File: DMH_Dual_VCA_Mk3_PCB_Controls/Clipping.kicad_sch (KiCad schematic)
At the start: 48 parts, among them Q10 BC548, Q11 BC548, Q12 BC548, Q9 BC548, SW2 SW_DPDT_OnOffOn_x2, U10 TL074

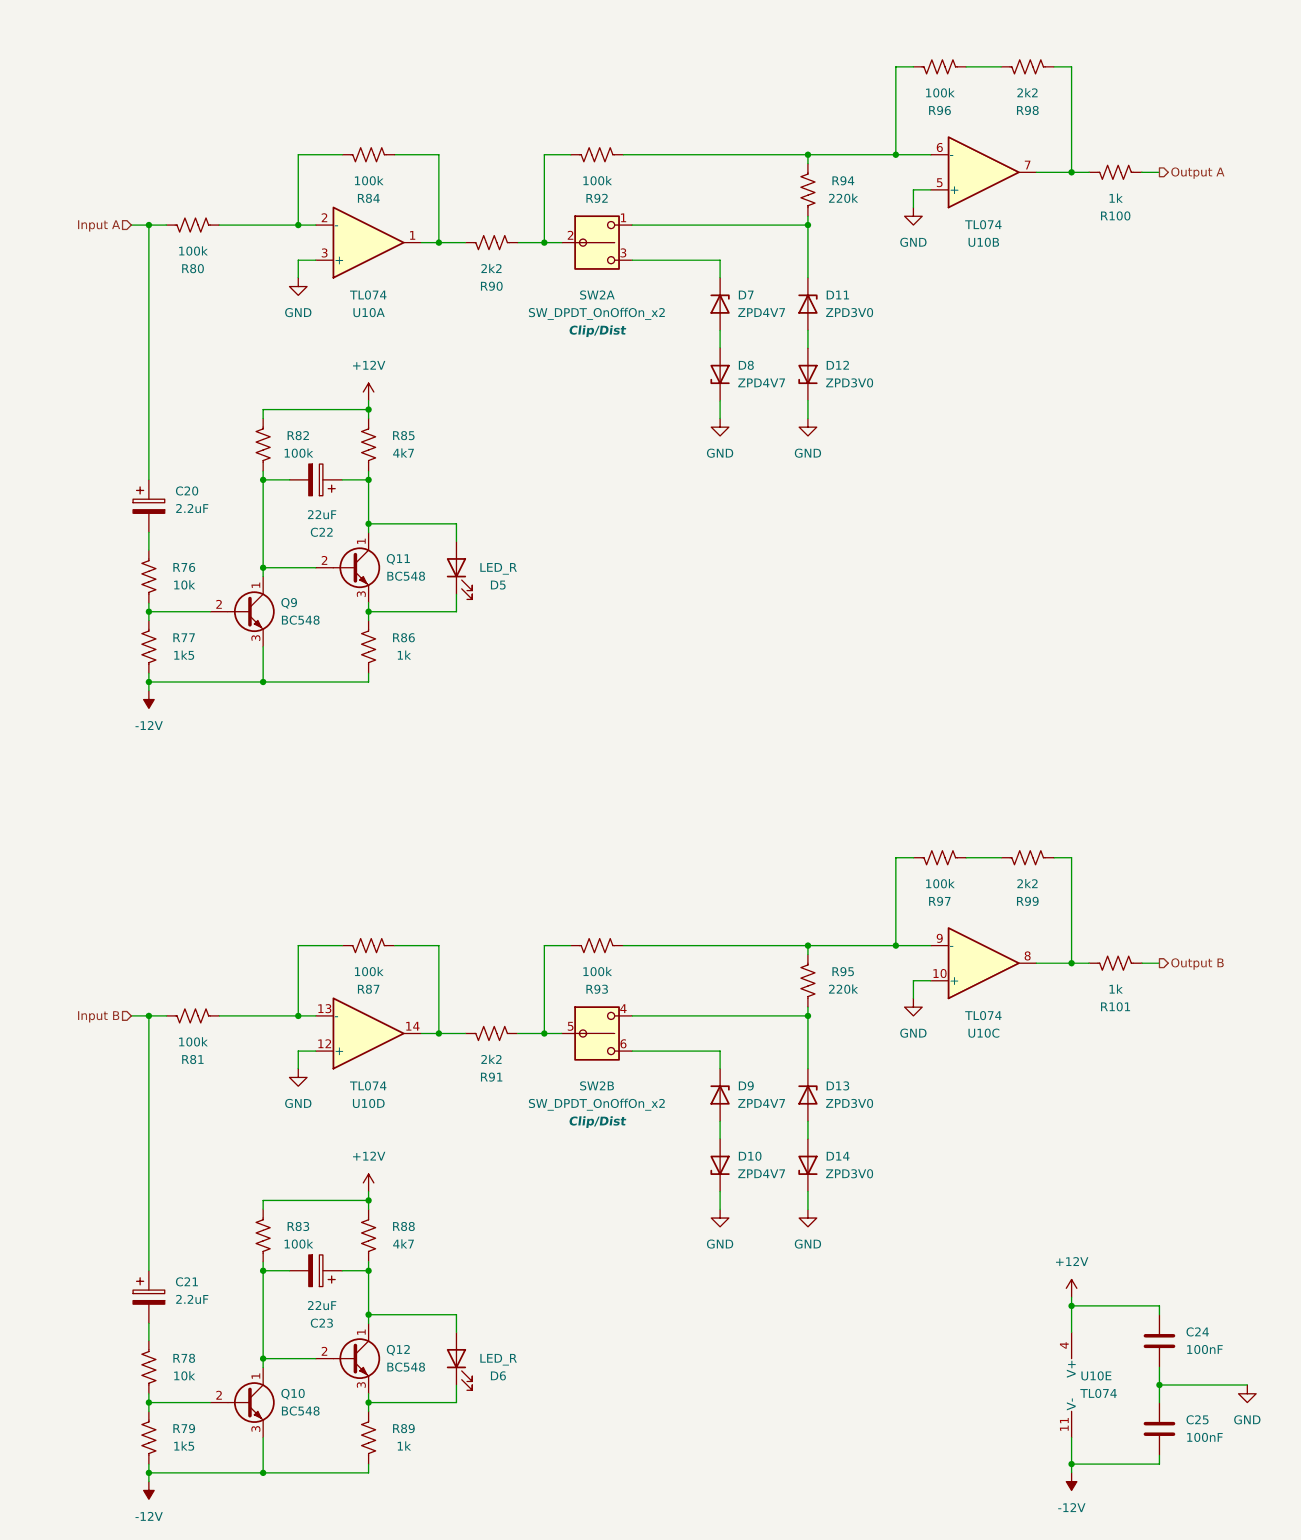
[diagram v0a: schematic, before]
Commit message: Moved clipping circuit back to main PCB
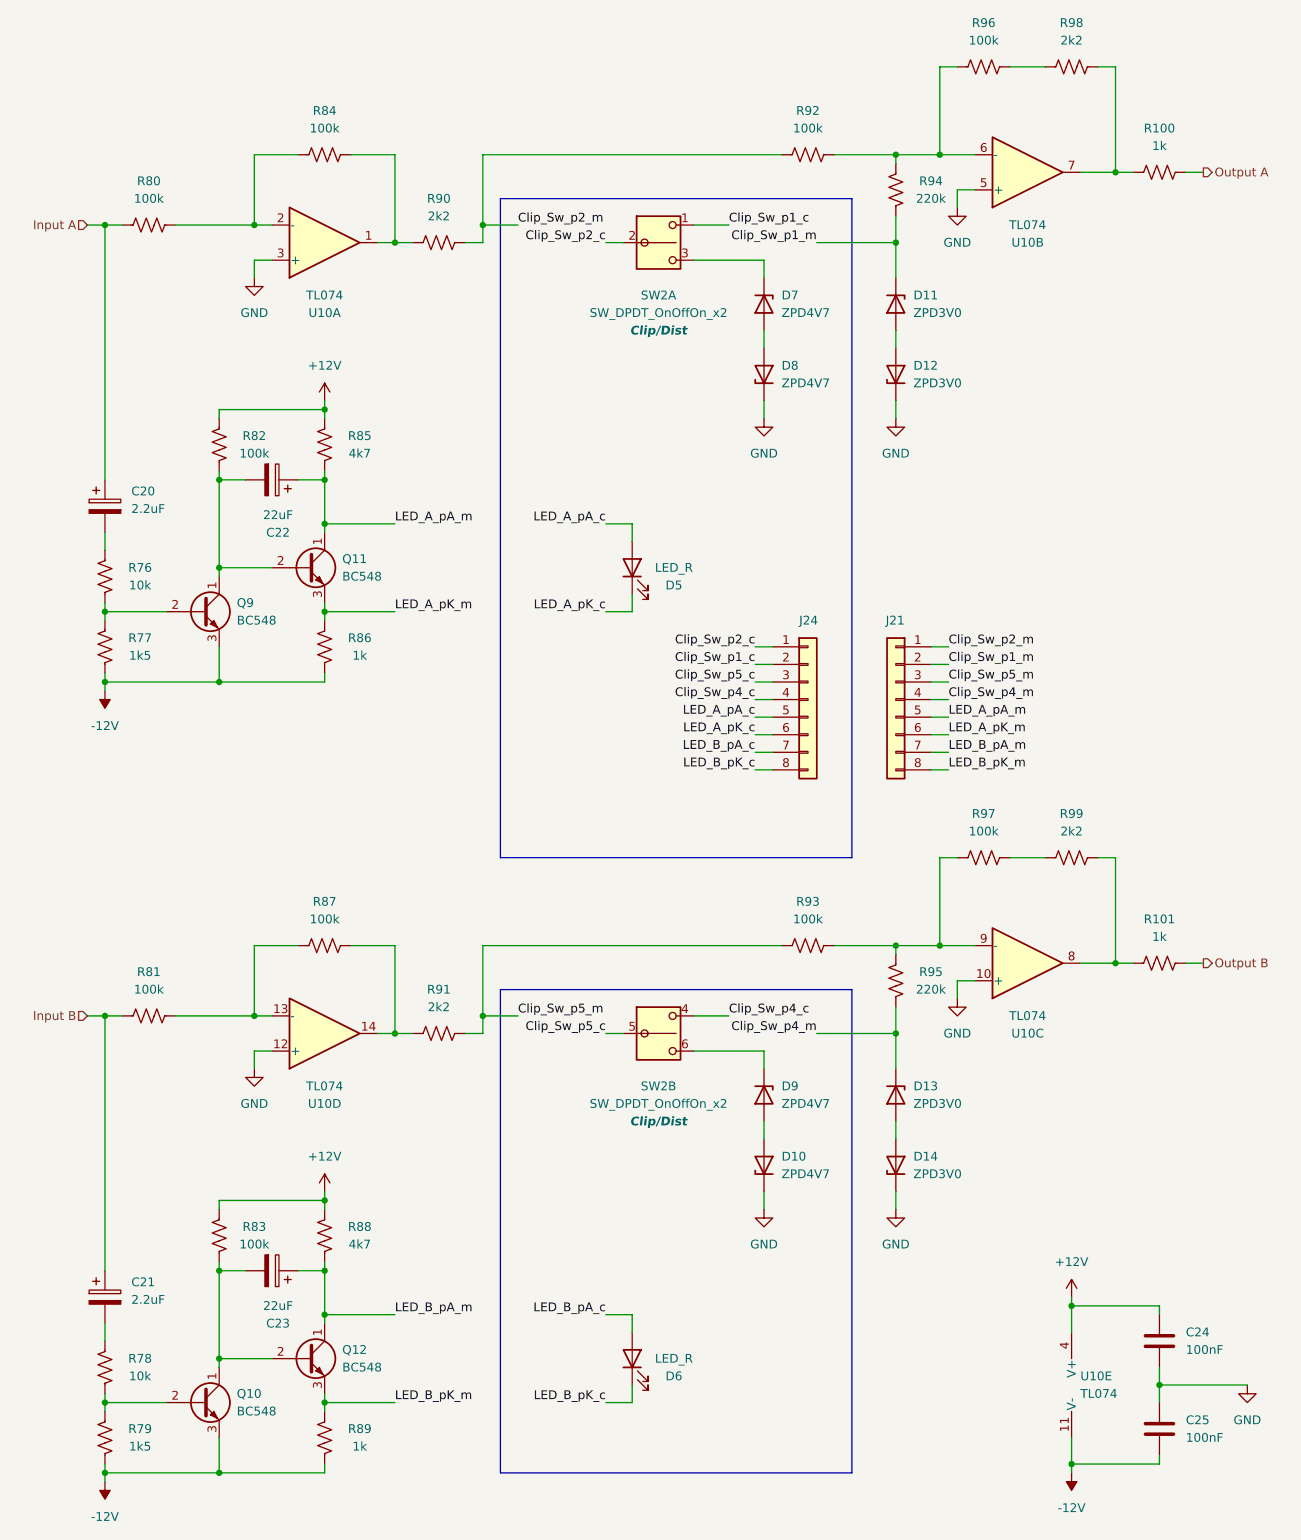
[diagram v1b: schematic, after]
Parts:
- added J21: Conn_01x08, Connector_PinHeader_2.54mm:PinHeader_1x08_P2.54mm_Vertical, symbol Connector_Generic:Conn_01x08
- added J24: Conn_01x08, Connector_PinSocket_2.54mm:PinSocket_1x08_P2.54mm_Vertical, symbol Connector_Generic:Conn_01x08
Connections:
- net Clip_Sw_p5_m: now reaches R91.2, R93.1
- net Clip_Sw_p5_m: now also J21.3 (Pin_3); no longer SW2.5 (B)
- net LED_A_pA_m: now reaches C22.1, Q11.1 (C), R85.1
- net LED_A_pA_m: now also J21.5 (Pin_5); no longer D5.2 (A)
- net LED_B_pK_m: now reaches Q12.3 (E), R89.2
- net LED_B_pK_m: now also J21.8 (Pin_8); no longer D6.1 (K)
- net Clip_Sw_p2_m: now reaches R90.2, R92.1
- net Clip_Sw_p2_m: now also J21.1 (Pin_1); no longer SW2.2 (B)
- net LED_B_pA_m: now reaches C23.1, Q12.1 (C), R88.1
- net LED_B_pA_m: now also J21.7 (Pin_7); no longer D6.2 (A)
- net LED_A_pK_m: now reaches Q11.3 (E), R86.2
- net LED_A_pK_m: now also J21.6 (Pin_6); no longer D5.1 (K)
- net Clip_Sw_p1_m: now reaches D11.1 (K), R94.1
- net Clip_Sw_p1_m: now also J21.2 (Pin_2); no longer SW2.1 (A)
- net Clip_Sw_p4_m: now reaches D13.1 (K), R95.1
- net Clip_Sw_p4_m: now also J21.4 (Pin_4); no longer SW2.4 (A)
- new net Clip_Sw_p1_c: J24.2 (Pin_2), SW2.1 (A)
- new net Clip_Sw_p2_c: J24.1 (Pin_1), SW2.2 (B)
- new net Clip_Sw_p4_c: J24.4 (Pin_4), SW2.4 (A)
- new net Clip_Sw_p5_c: J24.3 (Pin_3), SW2.5 (B)
- new net LED_A_pA_c: D5.2 (A), J24.5 (Pin_5)
- new net LED_A_pK_c: D5.1 (K), J24.6 (Pin_6)
- new net LED_B_pA_c: D6.2 (A), J24.7 (Pin_7)
- new net LED_B_pK_c: D6.1 (K), J24.8 (Pin_8)
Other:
- moved on the sheet: C20, C21, C22, C23, D10, D11, D12, D13, D14, D5, D6, D7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

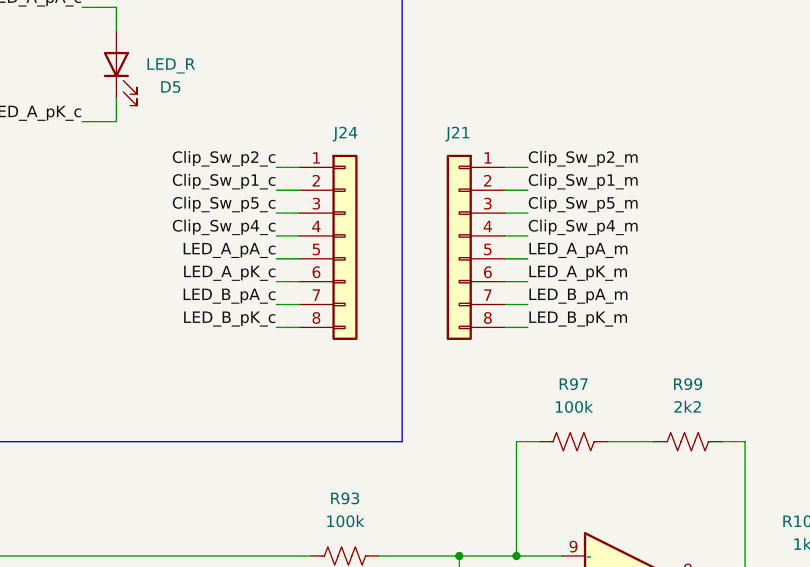
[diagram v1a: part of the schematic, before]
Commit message: Controls PCB comp placement in progress
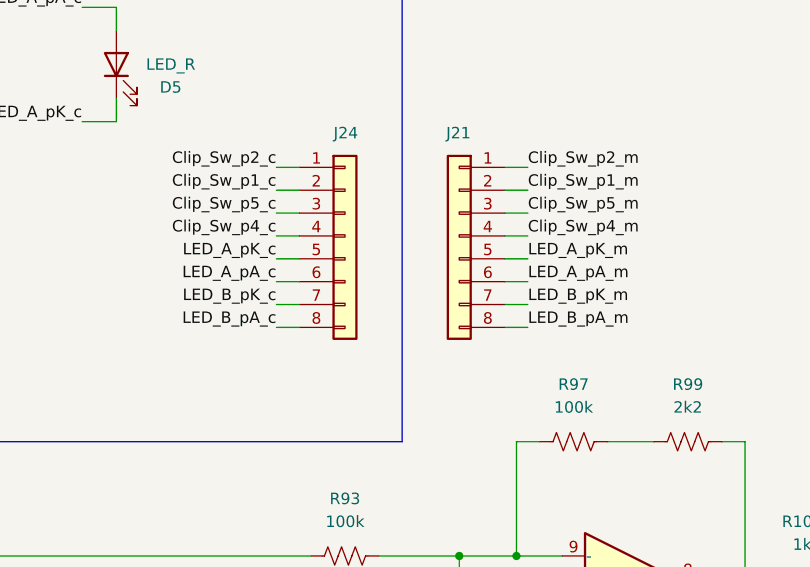
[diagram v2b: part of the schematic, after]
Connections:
- net LED_A_pA_c: now also J24.6 (Pin_6); no longer J24.5 (Pin_5)
- net LED_A_pA_m: now also J21.6 (Pin_6); no longer J21.5 (Pin_5)
- net LED_A_pK_c: now also J24.5 (Pin_5); no longer J24.6 (Pin_6)
- net LED_A_pK_m: now also J21.5 (Pin_5); no longer J21.6 (Pin_6)
- net LED_B_pA_c: now also J24.8 (Pin_8); no longer J24.7 (Pin_7)
- net LED_B_pA_m: now also J21.8 (Pin_8); no longer J21.7 (Pin_7)
- net LED_B_pK_c: now also J24.7 (Pin_7); no longer J24.8 (Pin_8)
- net LED_B_pK_m: now also J21.7 (Pin_7); no longer J21.8 (Pin_8)
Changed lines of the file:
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@@
 	)
 	(label "LED_B_pK_c"
-		(at 119.38 139.7 180)
+		(at 119.38 137.16 180)
 		(effects
 			(font
@@
 	)
 	(label "LED_A_pK_m"
-		(at 147.32 134.62 0)
+		(at 147.32 132.08 0)
 		(effects
 			(font
@@
 	)
 	(label "LED_B_pA_c"
-		(at 119.38 137.16 180)
+		(at 119.38 139.7 180)
 		(effects
 			(font
@@
 	)
 	(label "LED_B_pA_m"
-		(at 147.32 137.16 0)
+		(at 147.32 139.7 0)
 		(effects
 			(font
@@
 	)
 	(label "LED_A_pA_c"
+		(at 119.38 134.62 180)
+		(effects
+			(font
+				(size 1.27 1.27)
+			)
+			(justify right bottom)
+		)
+	)
+	(label "LED_B_pK_m"
+		(at 147.32 137.16 0)
+		(effects
+			(font
+				(size 1.27 1.27)
+			)
+			(justify left bottom)
+		)
+	)
+	(label "LED_A_pK_c"
 		(at 119.38 132.08 180)
 		(effects
@@
 		)
 	)
-	(label "LED_B_pK_m"
-		(at 147.32 139.7 0)
-		(effects
-			(font
-				(size 1.27 1.27)
-			)
-			(justify left bottom)
-		)
-	)
-	(label "LED_A_pK_c"
-		(at 119.38 134.62 180)
-		(effects
-			(font
-				(size 1.27 1.27)
-			)
-			(justify right bottom)
-		)
-	)
 	(label "LED_A_pA_m"
-		(at 147.32 132.08 0)
-		(effects
-			(font
+		(at 147.32 134.62 0)
+		(effects
+			(font
